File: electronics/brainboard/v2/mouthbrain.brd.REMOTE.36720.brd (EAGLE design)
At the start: 76.8 x 53.3 mm, 29 parts, among them Q1 MOSFET-NCHANNELSMD, Q10 MOSFET-NCHANNELSMD, Q11 MOSFET-NCHANNELSMD, Q12 MOSFET-NCHANNELSMD, Q13 MOSFET-NCHANNELSMD, Q14 MOSFET-NCHANNELSMD, Q15 MOSFET-NCHANNELSMD, Q16 MOSFET-NCHANNELSMD, Q2 MOSFET-NCHANNELSMD, Q3 MOSFET-NCHANNELSMD, Q4 MOSFET-NCHANNELSMD, Q5 MOSFET-NCHANNELSMD, Q6 MOSFET-NCHANNELSMD, Q7 MOSFET-NCHANNELSMD, Q8 MOSFET-NCHANNELSMD, Q9 MOSFET-NCHANNELSMD, U1 MCP4352, U2 MCP4352, U3 MCP4352, U4 MCP4352, U5 MOSFET-NCHANNEL-SOIC8

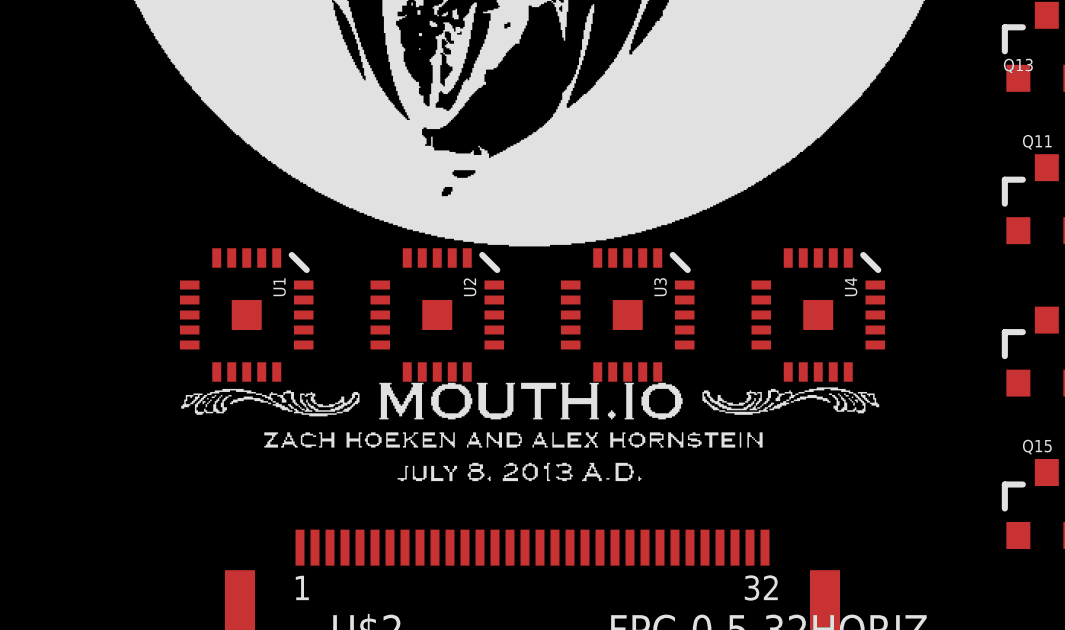
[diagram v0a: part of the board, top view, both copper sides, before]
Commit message: switched ADCs to package with ground pad
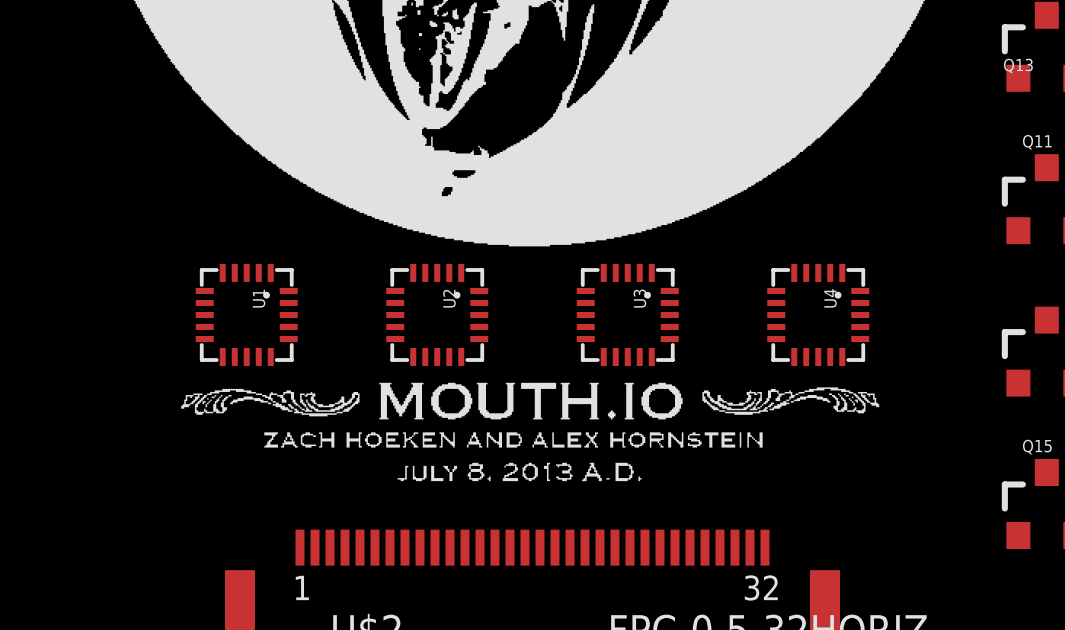
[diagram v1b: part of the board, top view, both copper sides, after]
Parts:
- U1, U2, U3, U4: device mouthbrain:QFN-20-PAD -> mouthbrain:QFN-20
